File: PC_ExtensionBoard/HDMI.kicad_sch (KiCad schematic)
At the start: 1 part

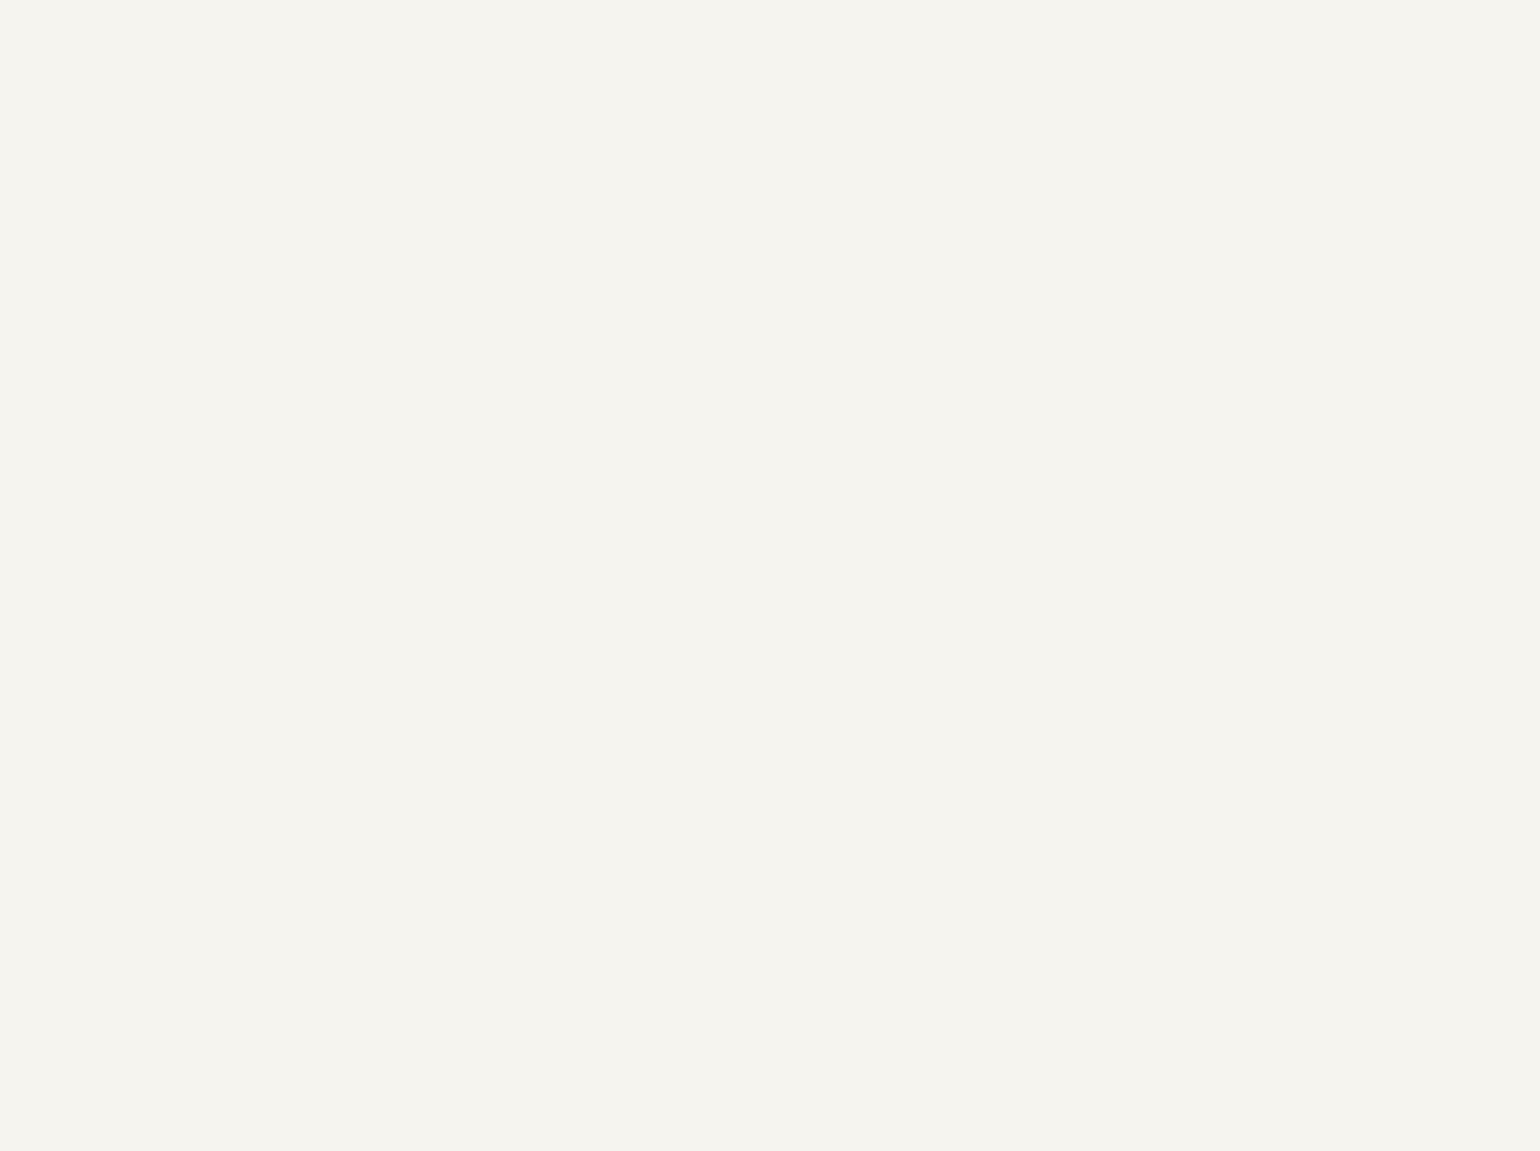
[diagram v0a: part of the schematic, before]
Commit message: update schematic: add pattern
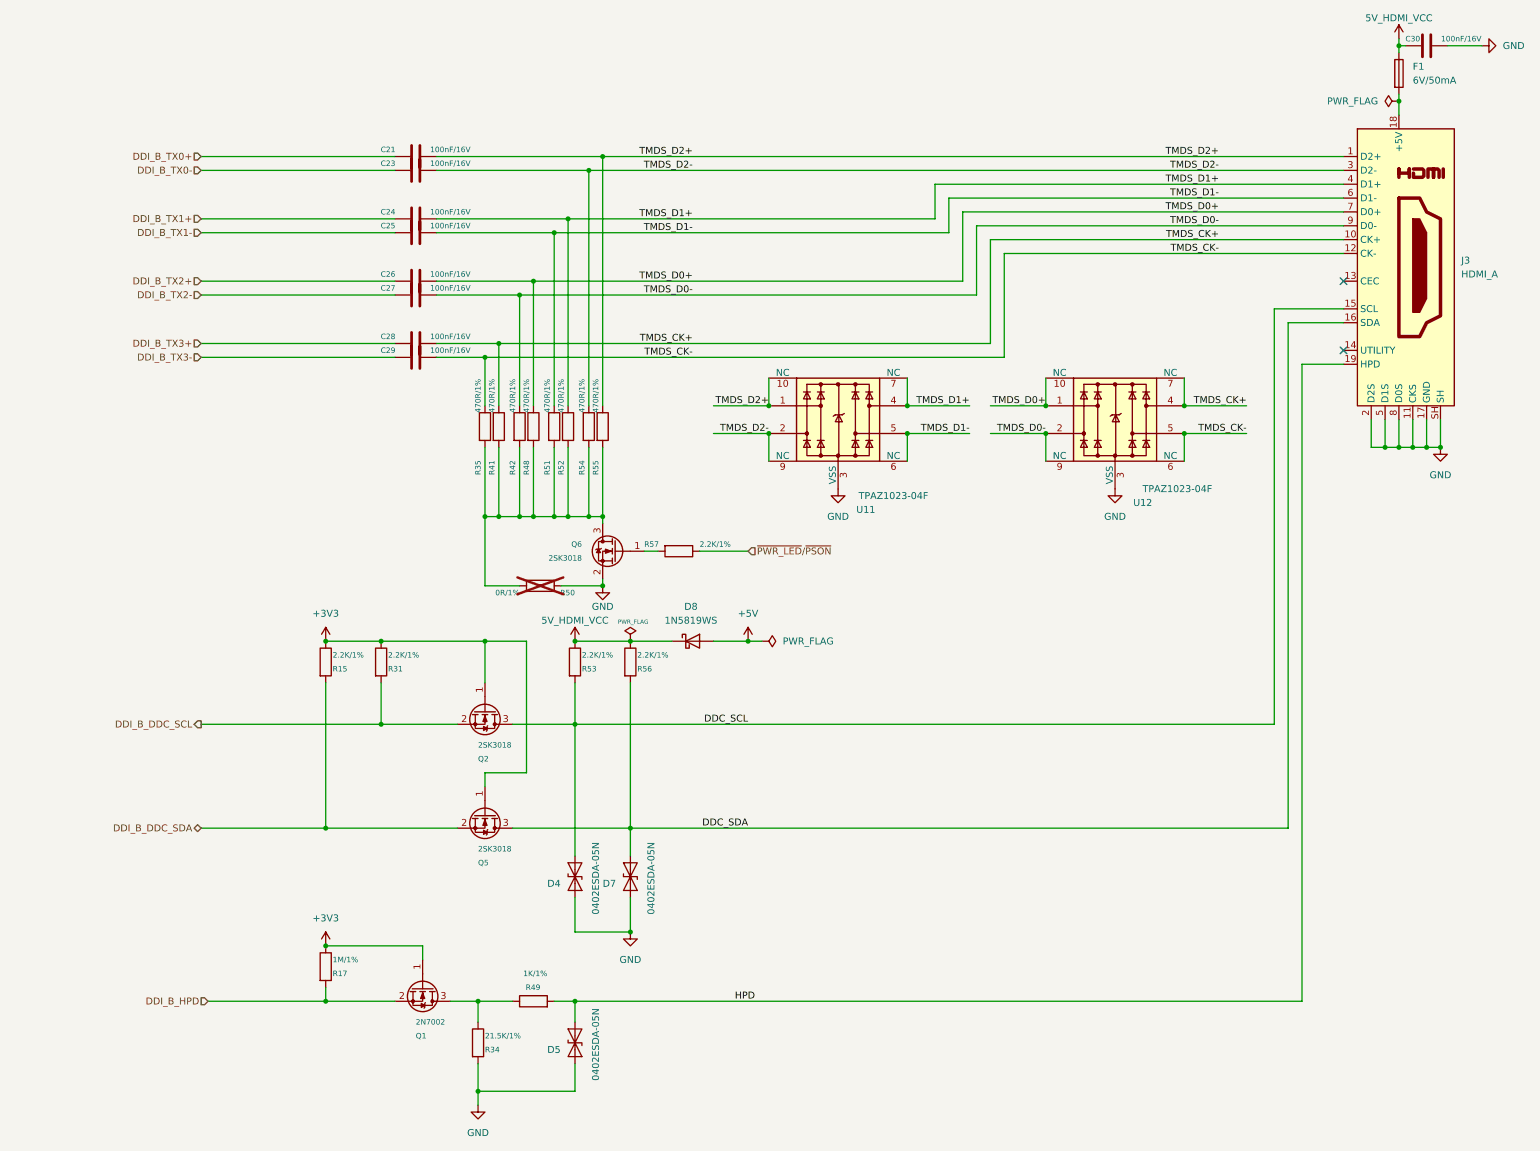
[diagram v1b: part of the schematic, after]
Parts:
- added C21, C23, C24, C25, C26, C27, C28, C29, C30: 100nF/16V, A_HDJ_Library:C_0402_1005Metric, symbol Device:C
- added D4, D5, D7: 0402ESDA-05N, A_HDJ_Library:D_0402_1005Metric, symbol Diode:ESD9B5.0ST5G
- added D8: 1N5819WS, A_DFRobot:D_SOD-323, symbol Diode:1N5819WS
- added F1: 6V/50mA, A_HDJ_Library:R_0603_1608Metric, symbol Device:Fuse
- added J3: HDMI_A, A_HDJ_Library:HDMI_A_Molex_208658-1001_Horizontal, symbol Connector:HDMI_A
- added Q1: 2N7002, Package_TO_SOT_SMD:SOT-23, symbol Transistor_FET:2N7002
- added Q2, Q5, Q6: 2SK3018, Package_TO_SOT_SMD:SOT-23, symbol Transistor_FET:2N7002
- added R15, R31, R53, R56, R57: 2.2K/1%, A_DFRobot:R_0402, symbol Device:R
- added R17: 1M/1%, A_DFRobot:R_0402, symbol Device:R
- added R34: 21.5K/1%, A_DFRobot:R_0402, symbol Device:R
- added R35, R41, R42, R48, R51, R52, R54, R55: 470R/1%, A_DFRobot:R_0402, symbol Device:R
- added R49: 1K/1%, A_DFRobot:R_0402, symbol Device:R
- added R50: 0R/1%, A_HDJ_Library:R_0402_1005Metric, symbol Device:R
- added U11, U12: TPAZ1023-04F, A_HDJ_Library:Diodes_UDFN-10_1.0x2.5mm_P0.5mm, symbol Power_Protection:D3V3XA4B10LP
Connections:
- new net: Q6.3 (D), R35.2, R41.2, R42.2, R48.2, R50.1, R51.2, R52.2, R54.2, R55.2
- new net: Q1.3 (D), R34.1, R49.1
- new net: Q6.1 (G), R57.2
- new net: F1.2, J3.18 (+5V)
- new net +3V3: Q1.1 (G), Q2.1 (G), Q5.1 (G), R15.1, R17.1, R31.1
- new net +5V: D8.2 (A)
- new net 5V_HDMI_VCC: C30.1, D8.1 (K), F1.1, R53.1, R56.1
- new net DDC_SCL: D4.2 (A2), J3.15 (SCL), Q2.3 (D), R53.2
- new net DDC_SDA: D7.2 (A2), J3.16 (SDA), Q5.3 (D), R56.2
- new net DDI_B_DDC_SCL: Q2.2 (S), R31.2
- new net DDI_B_DDC_SDA: Q5.2 (S), R15.2
- new net DDI_B_HPD: Q1.2 (S), R17.2
- new net DDI_B_TX0+: C21.1
- new net DDI_B_TX0-: C23.1
- new net DDI_B_TX1+: C24.1
- new net DDI_B_TX1-: C25.1
- new net DDI_B_TX2+: C26.1
- new net DDI_B_TX2-: C27.1
- new net DDI_B_TX3+: C28.1
- new net DDI_B_TX3-: C29.1
- new net GND: C30.2, D4.1 (A1), D5.1 (A1), D7.1 (A1), J3.11 (CKS), J3.17 (GND), J3.2 (D2S), J3.5 (D1S), J3.8 (D0S), J3.SH, Q6.2 (S), R34.2, R50.2, U11.3 (VSS), U11.8 (VSS), U12.3 (VSS), U12.8 (VSS)
- new net HPD: D5.2 (A2), J3.19 (HPD), R49.2
- new net TMDS_CK+: C28.2, J3.10 (CK+), R41.1, U12.4, U12.7 (NC)
- new net TMDS_CK-: C29.2, J3.12 (CK-), R35.1, U12.5, U12.6 (NC)
- new net TMDS_D0+: C26.2, J3.7 (D0+), R48.1, U12.1, U12.10 (NC)
- new net TMDS_D0-: C27.2, J3.9 (D0-), R42.1, U12.2, U12.9 (NC)
- new net TMDS_D1+: C24.2, J3.4 (D1+), R52.1, U11.4, U11.7 (NC)
- new net TMDS_D1-: C25.2, J3.6 (D1-), R51.1, U11.5, U11.6 (NC)
- new net TMDS_D2+: C21.2, J3.1 (D2+), R55.1, U11.1, U11.10 (NC)
- new net TMDS_D2-: C23.2, J3.3 (D2-), R54.1, U11.2, U11.9 (NC)
- new net ~{PWR_LED}/~{PSON}: R57.1
- no-connect marks 0 -> 2

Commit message: update schematic
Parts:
- removed HDMI1: HDMI-019S, ACLAB:HDMI-SMD_HDMI-019S, symbol ACLAB_Symbol:root_0_HDMI-019S_
- HDMI1: renamed from J3; DF_Comment 直插式HDMI母座-19Pin(19PIN) -> (none); LCSC (none) -> C111617
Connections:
- net DDI_B_DDC_SCL renamed DDI1.SCL
- net DDI_B_DDC_SDA renamed DDI1.SDA
- net DDI_B_HPD renamed DDI1_HPD
- net DDI_B_TX0+ renamed DDI1.TX0+
- net DDI_B_TX0- renamed DDI1.TX0-
- net DDI_B_TX1+ renamed DDI1.TX1+
- net DDI_B_TX1- renamed DDI1.TX1-
- net DDI_B_TX2+ renamed DDI1.TX2+
- net DDI_B_TX2- renamed DDI1.TX2-
- net DDI_B_TX3+ renamed DDI1.TX3+
- net DDI_B_TX3- renamed DDI1.TX3-
- new net: HDMI1.20 (SHD), HDMI1.21 (SHD), HDMI1.22 (SHD), HDMI1.23 (SHD)
- no-connect marks 2 -> 3

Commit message: refactor project
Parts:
- removed C21, C23, C24, C25, C26, C27, C28, C29: 100nF/16V, A_HDJ_Library:C_0402_1005Metric, symbol Device:C
- removed D4, D5, D7: 0402ESDA-05N, A_HDJ_Library:D_0402_1005Metric, symbol Diode:ESD9B5.0ST5G
- removed D8: 1N5819WS, A_DFRobot:D_SOD-323, symbol Diode:1N5819WS
- removed HDMI1: HDMI_A, A_HDJ_Library:HDMI_A_Molex_208658-1001_Horizontal, symbol Connector:HDMI_A
- removed Q1: 2N7002, Package_TO_SOT_SMD:SOT-23, symbol Transistor_FET:2N7002
- removed Q2, Q5, Q6: 2SK3018, Package_TO_SOT_SMD:SOT-23, symbol Transistor_FET:2N7002
- removed R15, R31, R53, R56, R57: 2.2K/1%, A_DFRobot:R_0402, symbol Device:R
- removed R17: 1M/1%, A_DFRobot:R_0402, symbol Device:R
- removed R34: 21.5K/1%, A_DFRobot:R_0402, symbol Device:R
- removed R35, R41, R42, R48, R51, R52, R54, R55: 470R/1%, A_DFRobot:R_0402, symbol Device:R
- removed R49: 1K/1%, A_DFRobot:R_0402, symbol Device:R
- removed R50: 0R/1%, A_HDJ_Library:R_0402_1005Metric, symbol Device:R
- removed U11, U12: TPAZ1023-04F, A_HDJ_Library:Diodes_UDFN-10_1.0x2.5mm_P0.5mm, symbol Power_Protection:D3V3XA4B10LP
- added C1, C19, C2, C20, C3, C4, C8, C9: 100nF/16V, A_HDJ_Library:C_0402_1005Metric, symbol A_PC_ExtensionBoard:C
- added D1: 1N5819WS, A_DFRobot:D_SOD-323, symbol A_PC_ExtensionBoard:1N5819WS
- added D2, D4, D7: 0402ESDA-05N, A_HDJ_Library:D_0402_1005Metric, symbol A_PC_ExtensionBoard:ESD9B5.0ST5G
- added HDMI1: HDMI_A, A_HDJ_Library:HDMI_A_Molex_208658-1001_Horizontal, symbol A_PC_ExtensionBoard:HDMI_A
- added Q10, Q6, Q9: 2SK3018, Package_TO_SOT_SMD:SOT-23, symbol A_PC_ExtensionBoard:2N7002
- added Q11: 2N7002, Package_TO_SOT_SMD:SOT-23, symbol A_PC_ExtensionBoard:2N7002
- added R12, R13, R18, R19, R20, R21, R22, R23: 470R/1%, symbol A_PC_ExtensionBoard:R
- added R24: 0R/1%, symbol A_PC_ExtensionBoard:R
- added R25, R28, R29, R31, R35: 2.2K/1%, symbol A_PC_ExtensionBoard:R
- added R41: 1M/1%, symbol A_PC_ExtensionBoard:R
- added R42: 21.5K/1%, symbol A_PC_ExtensionBoard:R
- added R48: 1K/1%, symbol A_PC_ExtensionBoard:R
- added U5, U6: TPAZ1023-04F, A_HDJ_Library:Diodes_UDFN-10_1.0x2.5mm_P0.5mm, symbol A_PC_ExtensionBoard:D3V3XA4B10LP
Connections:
- net +3V3: now also Q10.1 (G), Q11.1 (G), Q9.1 (G), R31.1, R35.1, R41.1
- net +5V: now also D1.2 (A)
- net 5V_HDMI_VCC: now also D1.1 (K), R28.1, R29.1
- net DDC_SCL: now also D2.2 (A2), HDMI1.15 (SCL), Q9.3 (D), R29.2
- net DDC_SDA: now also D4.2 (A2), HDMI1.16 (SDA), Q10.3 (D), R28.2
- net DDI1.SCL: now also Q9.2 (S), R35.2
- net DDI1.SDA: now also Q10.2 (S), R31.2
- net DDI1.TX0+: now also C1.1
- net DDI1.TX0-: now also C2.1
- net DDI1.TX1+: now also C3.1
- net DDI1.TX1-: now also C4.1
- net DDI1.TX2+: now also C8.1
- net DDI1.TX2-: now also C9.1
- net DDI1.TX3+: now also C19.1
- net DDI1.TX3-: now also C20.1
- net DDI1_HPD: now also Q11.2 (S), R41.2
- net GND: now also D2.1 (A1), D4.1 (A1), D7.1 (A1), HDMI1.11 (CKS), HDMI1.17 (GND), HDMI1.2 (D2S), HDMI1.5 (D1S), HDMI1.8 (D0S), HDMI1.SH, Q6.3 (D), R24.2, R42.2, U5.3 (VSS), U5.8 (VSS), U6.3 (VSS), U6.8 (VSS)
- net HPD: now also D7.2 (A2), HDMI1.19 (HPD), R48.2
- net TMDS_CK+: now also C19.2, HDMI1.10 (CK+), R13.1, U5.4, U5.7 (NC)
- net TMDS_CK-: now also C20.2, HDMI1.12 (CK-), R12.1, U5.5, U5.6 (NC)
- net TMDS_D0+: now also C8.2, HDMI1.7 (D0+), R19.1, U5.1, U5.10 (NC)
- net TMDS_D0-: now also C9.2, HDMI1.9 (D0-), R18.1, U5.2, U5.9 (NC)
- net TMDS_D1+: now also C3.2, HDMI1.4 (D1+), R21.1, U6.4, U6.7 (NC)
- net TMDS_D1-: now also C4.2, HDMI1.6 (D1-), R20.1, U6.5, U6.6 (NC)
- net TMDS_D2+: now also C1.2, HDMI1.1 (D2+), R23.1, U6.1, U6.10 (NC)
- net TMDS_D2-: now also C2.2, HDMI1.3 (D2-), R22.1, U6.2, U6.9 (NC)
- net ~{PWR_LED}/~{PSON}: now also R25.1
- net at F1.2: now also HDMI1.18 (+5V)
- new net: HDMI1.20 (SHD), HDMI1.21 (SHD), HDMI1.22 (SHD), HDMI1.23 (SHD)
- new net: Q6.2 (S), R12.2, R13.2, R18.2, R19.2, R20.2, R21.2, R22.2, R23.2, R24.1
- new net: Q11.3 (D), R42.1, R48.1
- new net: Q6.1 (G), R25.2

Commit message: re-link symbol
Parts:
- C1, C2, C3, C4, C8, C9: footprint A_HDJ_Library:C_0402_1005Metric -> Capacitor_SMD:C_0402_1005Metric
- D1: footprint A_DFRobot:D_SOD-323 -> PC_Components_1:SOT-323
- F1: footprint A_HDJ_Library:R_0603_1608Metric -> PC_Components_1:R_0603_1608Metric
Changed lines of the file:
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@@
 			)
 		)
-		(property "Footprint" "A_DFRobot:D_SOD-323"
+		(property "Footprint" "PC_Components_1:SOT-323"
 			(at 347.98 163.195 0)
 			(hide yes)
@@
 			)
 		)
-		(property "Footprint" "A_HDJ_Library:C_0402_1005Metric"
+		(property "Footprint" "Capacitor_SMD:C_0402_1005Metric"
 			(at 300.99 80.3148 0)
 			(hide yes)
@@
 			)
 		)
-		(property "Footprint" "A_HDJ_Library:R_0603_1608Metric"
+		(property "Footprint" "PC_Components_1:R_0603_1608Metric"
 			(at 475.742 54.61 90)
 			(hide yes)
@@
 			)
 		)
-		(property "Footprint" "A_HDJ_Library:C_0402_1005Metric"
+		(property "Footprint" "Capacitor_SMD:C_0402_1005Metric"
 			(at 300.99 82.8548 0)
 			(hide yes)
@@
 			)
 		)
-		(property "Footprint" "A_HDJ_Library:C_0402_1005Metric"
+		(property "Footprint" "Capacitor_SMD:C_0402_1005Metric"
 			(at 300.99 94.2848 0)
 			(hide yes)
@@
 			)
 		)
-		(property "Footprint" "A_HDJ_Library:C_0402_1005Metric"
+		(property "Footprint" "Capacitor_SMD:C_0402_1005Metric"
 			(at 300.99 68.8848 0)
 			(hide yes)
@@
 			)
 		)
-		(property "Footprint" "A_HDJ_Library:C_0402_1005Metric"
+		(property "Footprint" "Capacitor_SMD:C_0402_1005Metric"
 			(at 300.99 71.4248 0)
 			(hide yes)
@@
 			)
 		)
-		(property "Footprint" "A_HDJ_Library:C_0402_1005Metric"
+		(property "Footprint" "Capacitor_SMD:C_0402_1005Metric"
 			(at 300.99 91.7448 0)
 			(hide yes)
